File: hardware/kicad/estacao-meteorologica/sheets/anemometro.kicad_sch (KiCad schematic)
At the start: 12 parts, among them J31 R-RJ11R06P-A800, U40 SN74LVC1G17DBVR

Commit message: refatoracao: atualizacoes de hardware e falta revisao LoRa
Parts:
- added R42: 1k, Resistor_SMD:R_0603_1608Metric, symbol Device:R
- C40: value 10n -> 100n; Function Filtro do reed -> Filtro RC do reed com R41; suprime bounce e ruido de alta f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
- D41: Function Clamp secundario para GND e 3V3 -> Clamp secundario: p1=GND, p2=+3V3, p3=sinal filtrado
- J31: Function RJ11 individual; contatos centrais -> Conector do anemometro; reed externo entre p3 e p4; Rating 6P6C; p3=return; p4=signal; THT -> 6P6C; p3=+3V3 via R42; p4=sinal; THT
- R40: Function Pull-up ANTES do resistor serie; reed fechado ~0V -> Pull-down do sinal bruto; reed aberto = nivel baixo
- R41: Function Limitacao de corrente e filtro RC -> Resistor serie: limita corrente de clamp e, com C40, filtra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
- TP40: Function ANEMOMETRO_RAW -> Ponto de teste do sinal bruto ANEMOMETRO_RAW; LCSC (none) -> N/A (pad PCB); LCSC Part (none) -> N/A (pad PCB); MPN (none) -> TestPoint_Pad_D1.5mm; Manufacturer (none) -> PCB
- TP41: Function ANEMOMETRO_FILT -> Ponto de teste do sinal filtrado ANEMOMETRO_FILT; LCSC (none) -> N/A (pad PCB); LCSC Part (none) -> N/A (pad PCB); MPN (none) -> TestPoint_Pad_D1.5mm; Manufacturer (none) -> PCB
- TP42: Function WIND_SPEED_PULSE -> Ponto de teste da saida digital WIND_SPEED_PULSE; LCSC (none) -> N/A (pad PCB); LCSC Part (none) -> N/A (pad PCB); MPN (none) -> TestPoint_Pad_D1.5mm; Manufacturer (none) -> PCB
- TP43: Function GND -> Ponto de teste de referencia GND; LCSC (none) -> N/A (pad PCB); LCSC Part (none) -> N/A (pad PCB); MPN (none) -> TestPoint_Pad_D1.5mm; Manufacturer (none) -> PCB
- U40: Function Schmitt nao inversor; reed fecha -> borda de descida -> Schmitt nao inversor; reed fecha -> borda de subida em WIND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
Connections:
- net +3V3: now also R42.2; no longer R40.1
- net GND: now also R40.1; no longer J31.3
- new net: J31.3, R42.1
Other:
- note added: "1 CONECTOR / ESD / REFERENCIA"
- note added: "2 FILTRO / CLAMP SECUNDARIO"
- note added: "D40 deve ficar junto ao RJ11; R41, D41 e C40 junto ao U40. Manter plano GND continuo e retorno curto para D40. D40 e a protecao primaria do cabo; D41 apenas limita o residuo no buffer. Sem isolamento ou qualificacao contra raios: validar transitorios em bancada."
- note added: "Interface do sensor: J31.3 fornece +3V3 atraves de R42=1k; o reed externo fecha entre p3 e p4. R40=10k e o pull-down: reed aberto = 0 V; reed fechado = ~3,0 V e saida alta. C40=100n: tau de subida ~0,56 ms e de descida ~1,47 ms. PENDENCIA DE FIRMWARE: usar EXTI na subida e sem pull interno; o codigo atual ainda usa descida com pull-up. Debounce <= 6 ms para 75 Hz."
- note added: "MISOL: contato reed passivo; cabo externo ~2 m. J31 p3 = +3V3 via R42; J31 p4 = sinal."
- note removed: "1 CONECTOR / ESD"
- note removed: "2 FILTRO / CLAMP"
- note removed: "ESD junto ao RJ11; clamp e C junto ao buffer. Plano GND continuo. Protecao transitoria a validar em bancada; sem isolamento e sem qualificacao contra raios."
- note removed: "MISOL: contato reed passivo; cabo externo ~2 m; entrada individual 6P6C p3/p4."
- note removed: "Pull-up no lado do cabo evita divisor 4k7/10k na entrada Schmitt. Tau abertura=147 us; fechamento=47 us. Debounce atual: 20 ms limita f ~50 Hz. Com 2,4 km/h/Hz: 50 m/s exige 75 Hz; revisar debounce no firmware."
- moved on the sheet: R40, TP42, TP43

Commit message: refatoracao: lora + Verificacao projeto inteiro
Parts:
- C40: LCSC C57112 -> C14663; LCSC Part C57112 -> C14663; MPN 0603B103K500NT -> CC0603KRX7R9BB104; Manufacturer FH -> YAGEO; Modelo 3D (none) -> ${KICAD9_3DMODEL_DIR}/Capacitor_SMD.3dshapes/C_0603_1608Met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; Status_Ficha (none) -> Conferido no catalogo em 2026-09-24; verificar estoque ao c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
- C41: Modelo 3D (none) -> ${KICAD9_3DMODEL_DIR}/Capacitor_SMD.3dshapes/C_0603_1608Met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; Status_Ficha (none) -> Conferido no catalogo em 2026-09-24; verificar estoque ao c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
- D40: Modelo 3D (none) -> ${KICAD9_3DMODEL_DIR}/Diode_SMD.3dshapes/D_SOD-882.step; Status_Ficha (none) -> Conferido no catalogo em 2026-09-24; verificar estoque ao c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
- D41: Modelo 3D (none) -> ${KICAD9_3DMODEL_DIR}/Package_TO_SOT_SMD.3dshapes/SOT-23.st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; Status_Ficha (none) -> Conferido no catalogo em 2026-09-24; verificar estoque ao c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
- J31: Manufacturer Ckmtw -> Ckmtw(Shenzhen Cankemeng); Modelo 3D (none) -> ${KIPRJMOD}/../../libraries/Sensores_Meteo/Sensores_Meteo.3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; Status_Ficha (none) -> Conferido no catalogo em 2026-09-24; verificar estoque ao c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
- R40, R41: Manufacturer UNI-ROYAL -> UNI-ROYAL(Uniroyal Elec); Modelo 3D (none) -> ${KICAD9_3DMODEL_DIR}/Resistor_SMD.3dshapes/R_0603_1608Metr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; Status_Ficha (none) -> Conferido no catalogo em 2026-09-24; verificar estoque ao c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
- R42: LCSC C25804 -> C21190; LCSC Part C25804 -> C21190; MPN 0603WAF1002T5E -> 0603WAF1001T5E; Manufacturer UNI-ROYAL -> UNI-ROYAL(Uniroyal Elec); Modelo 3D (none) -> ${KICAD9_3DMODEL_DIR}/Resistor_SMD.3dshapes/R_0603_1608Metr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; Status_Ficha (none) -> Conferido no catalogo em 2026-09-24; verificar estoque ao c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
- TP40, TP41, TP42, TP43: LCSC N/A (pad PCB) -> N/A; LCSC Part N/A (pad PCB) -> N/A; MPN TestPoint_Pad_D1.5mm -> N/A - elemento de cobre da PCB; Manufacturer PCB -> N/A; Modelo 3D (none) -> N/A - geometria de cobre, sem corpo
- U40: Modelo 3D (none) -> ${KICAD9_3DMODEL_DIR}/Package_TO_SOT_SMD.3dshapes/SOT-23-5.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; Status_Ficha (none) -> Conferido no catalogo em 2026-09-24; verificar estoque ao c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

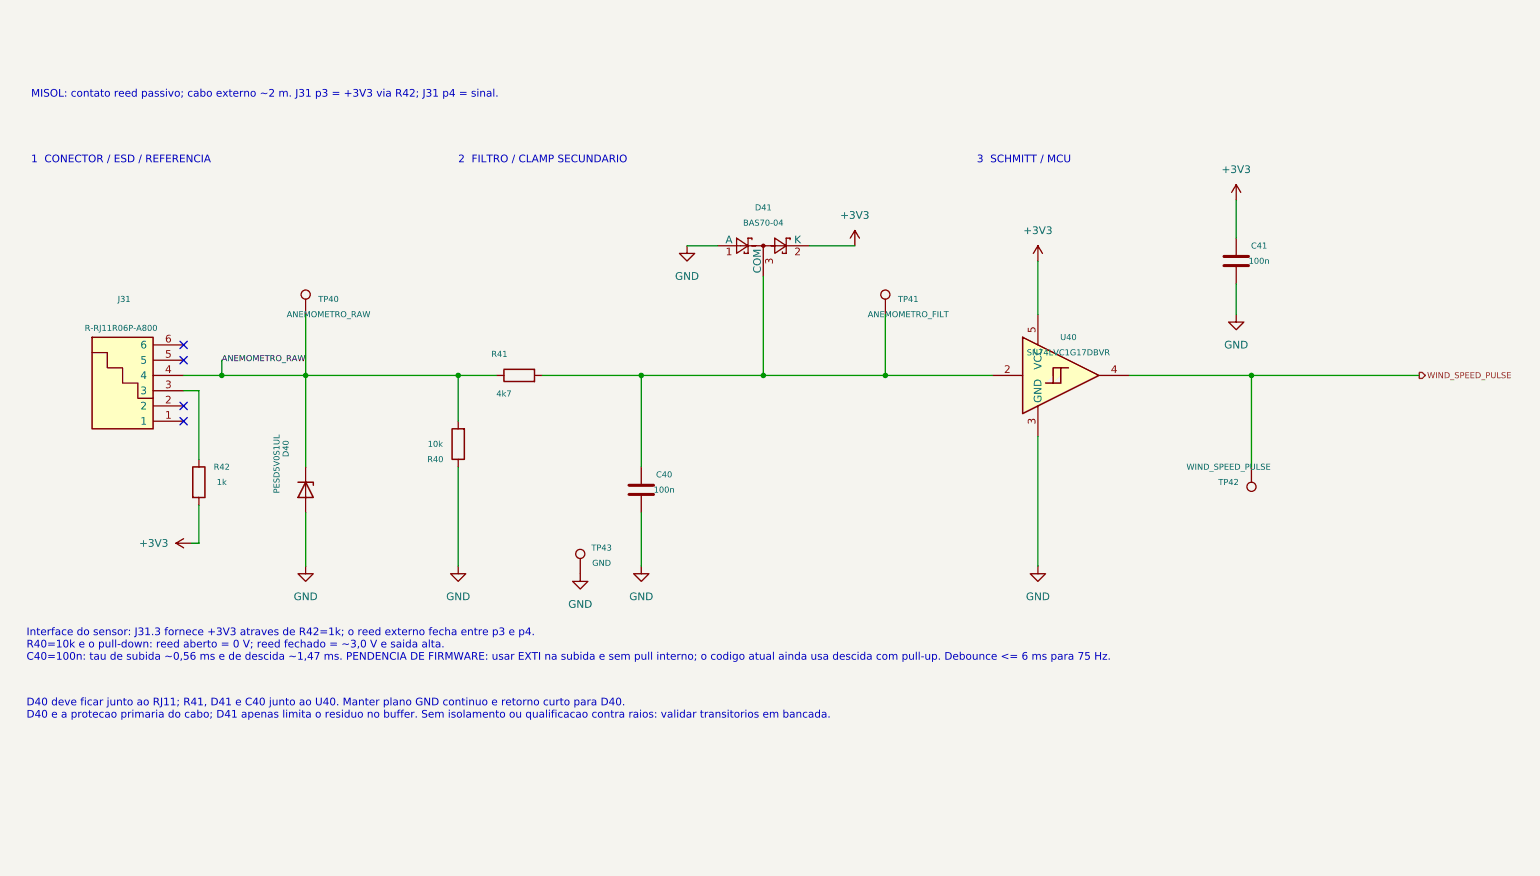
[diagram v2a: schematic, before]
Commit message: Padronizacao de nomes e numero de componentes
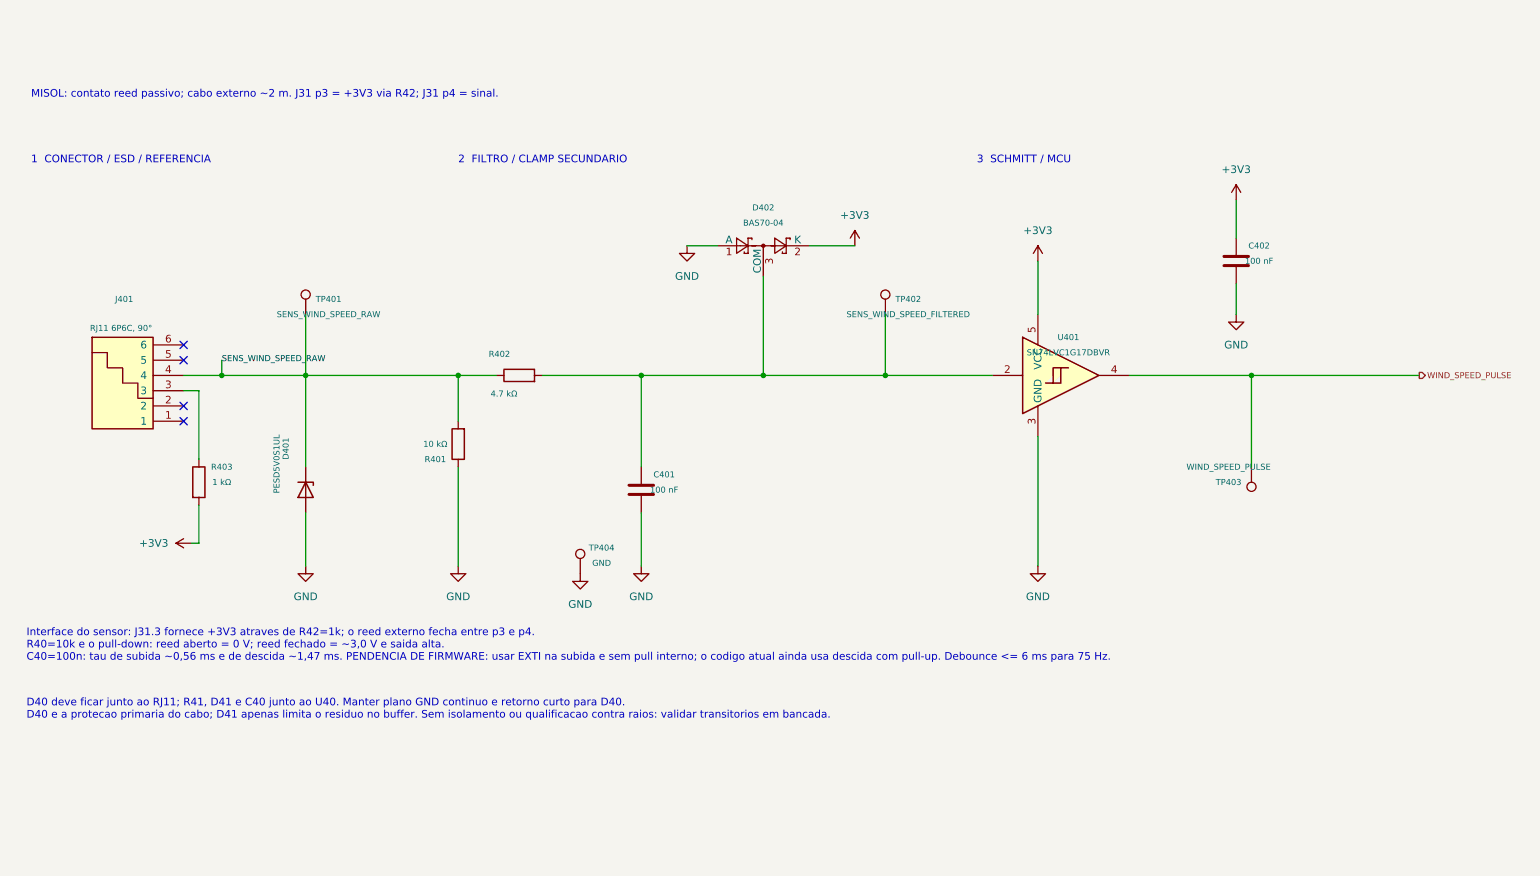
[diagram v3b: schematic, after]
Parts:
- C401: renamed from C40; value 100n -> 100 nF; Assembly (none) -> SMT; LCSC Part C14663 -> (none); Modelo 3D ${KICAD9_3DMODEL_DIR}/Capacitor_SMD.3dshapes/C_0603_1608Met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 -> (none); Rating 10%; 50V; X7R -> (none); Specification (none) -> 10%; 50V; X7R; Status_Ficha Conferido no catalogo em 2026-09-24; verificar estoque ao c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 -> (none); Verification (none) -> Conferido no catalogo em 2026-09-24; verificar estoque ao c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
- C402: renamed from C41; value 100n -> 100 nF; Assembly (none) -> SMT; LCSC Part C14663 -> (none); Modelo 3D ${KICAD9_3DMODEL_DIR}/Capacitor_SMD.3dshapes/C_0603_1608Met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 -> (none); Rating 10%; 50V; X7R -> (none); Specification (none) -> 10%; 50V; X7R; Status_Ficha Conferido no catalogo em 2026-09-24; verificar estoque ao c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 -> (none); Verification (none) -> Conferido no catalogo em 2026-09-24; verificar estoque ao c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
- D401: renamed from D40; Assembly (none) -> SMT; LCSC Part C85402 -> (none); Modelo 3D ${KICAD9_3DMODEL_DIR}/Diode_SMD.3dshapes/D_SOD-882.step -> (none); Rating VRWM=5V; IR max 1uA at 5V/25C; see datasheet -> (none); Specification (none) -> VRWM=5V; IR max 1uA at 5V/25C; see datasheet; Status_Ficha Conferido no catalogo em 2026-09-24; verificar estoque ao c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 -> (none); Verification (none) -> Conferido no catalogo em 2026-09-24; verificar estoque ao c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
- D402: renamed from D41; Assembly (none) -> SMT; LCSC Part C389351 -> (none); Modelo 3D ${KICAD9_3DMODEL_DIR}/Package_TO_SOT_SMD.3dshapes/SOT-23.st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 -> (none); Rating IR max 100nA at 50V/25C; 1=GND, 2=3V3, 3=signal -> (none); Specification (none) -> IR max 100nA at 50V/25C; 1=GND, 2=3V3, 3=signal; Status_Ficha Conferido no catalogo em 2026-09-24; verificar estoque ao c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 -> (none); Verification (none) -> Conferido no catalogo em 2026-09-24; verificar estoque ao c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
- J401: renamed from J31; value R-RJ11R06P-A800 -> RJ11 6P6C, 90°; Assembly (none) -> SMT; LCSC Part C189750 -> (none); Modelo 3D ${KIPRJMOD}/../../libraries/Sensores_Meteo/Sensores_Meteo.3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 -> (none); Rating 6P6C; p3=+3V3 via R42; p4=sinal; THT -> (none); Specification (none) -> 6P6C; p3=+3V3 via R42; p4=sinal; THT; Status_Ficha Conferido no catalogo em 2026-09-24; verificar estoque ao c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 -> (none); Verification (none) -> Conferido no catalogo em 2026-09-24; verificar estoque ao c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
- R401: renamed from R40; value 10k -> 10 kΩ; Assembly (none) -> SMT; LCSC Part C25804 -> (none); Modelo 3D ${KICAD9_3DMODEL_DIR}/Resistor_SMD.3dshapes/R_0603_1608Metr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 -> (none); Rating 1%; 0.1W; 75V -> (none); Specification (none) -> 1%; 0.1W; 75V; Status_Ficha Conferido no catalogo em 2026-09-24; verificar estoque ao c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 -> (none); Verification (none) -> Conferido no catalogo em 2026-09-24; verificar estoque ao c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
- R402: renamed from R41; value 4k7 -> 4.7 kΩ; Assembly (none) -> SMT; LCSC Part C23162 -> (none); Modelo 3D ${KICAD9_3DMODEL_DIR}/Resistor_SMD.3dshapes/R_0603_1608Metr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 -> (none); Rating 1%; 0.1W; 75V -> (none); Specification (none) -> 1%; 0.1W; 75V; Status_Ficha Conferido no catalogo em 2026-09-24; verificar estoque ao c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 -> (none); Verification (none) -> Conferido no catalogo em 2026-09-24; verificar estoque ao c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
- R403: renamed from R42; value 1k -> 1 kΩ; Assembly (none) -> SMT; LCSC Part C21190 -> (none); Modelo 3D ${KICAD9_3DMODEL_DIR}/Resistor_SMD.3dshapes/R_0603_1608Metr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 -> (none); Rating 1%; 0.1W; 75V -> (none); Specification (none) -> 1%; 0.1W; 75V; Status_Ficha Conferido no catalogo em 2026-09-24; verificar estoque ao c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 -> (none); Verification (none) -> Conferido no catalogo em 2026-09-24; verificar estoque ao c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
- TP401: renamed from TP40; value ANEMOMETRO_RAW -> SENS_WIND_SPEED_RAW; Assembly (none) -> PCB — sem compra; LCSC Part N/A -> (none); Modelo 3D N/A - geometria de cobre, sem corpo -> (none); Rating Copper pad; no purchased component -> (none); Specification (none) -> Copper pad; no purchased component
- TP402: renamed from TP41; value ANEMOMETRO_FILT -> SENS_WIND_SPEED_FILTERED; Assembly (none) -> PCB — sem compra; LCSC Part N/A -> (none); Modelo 3D N/A - geometria de cobre, sem corpo -> (none); Rating Copper pad; no purchased component -> (none); Specification (none) -> Copper pad; no purchased component
- TP403: renamed from TP42; Assembly (none) -> PCB — sem compra; LCSC Part N/A -> (none); Modelo 3D N/A - geometria de cobre, sem corpo -> (none); Rating Copper pad; no purchased component -> (none); Specification (none) -> Copper pad; no purchased component
- TP404: renamed from TP43; Assembly (none) -> PCB — sem compra; LCSC Part N/A -> (none); Modelo 3D N/A - geometria de cobre, sem corpo -> (none); Rating Copper pad; no purchased component -> (none); Specification (none) -> Copper pad; no purchased component
- U401: renamed from U40; Assembly (none) -> SMT; LCSC Part C7836 -> (none); Modelo 3D ${KICAD9_3DMODEL_DIR}/Package_TO_SOT_SMD.3dshapes/SOT-23-5.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 -> (none); Rating Non-inverting Schmitt; 1=NC 2=A 3=GND 4=Y 5=VCC -> (none); Specification (none) -> Non-inverting Schmitt; 1=NC 2=A 3=GND 4=Y 5=VCC; Status_Ficha Conferido no catalogo em 2026-09-24; verificar estoque ao c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 -> (none); Verification (none) -> Conferido no catalogo em 2026-09-24; verificar estoque ao c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
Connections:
- net ANEMOMETRO_RAW renamed SENS_WIND_SPEED_RAW

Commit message: Roteamento 2.0 - rj11 compartilhado biruta e anemometro
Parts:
- removed J401: RJ11 6P6C, 90°, Sensores_Meteo:RJ11-TH_PCB-6P6C-90, symbol Sensores_Meteo:PCB-6P6C-90
- removed R403: 1 kΩ, Resistor_SMD:R_0603_1608Metric, symbol Device:R
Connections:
- no-connect marks 4 -> 0

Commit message: Refact - mudança do sensor bh1750 para placa filha e conector jst + reposicionamento do sensor DHT22 para reduzir influencia de temperatura interna da placa
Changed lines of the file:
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@@
-	)
-	(junction
-		(at 52.07 80.01)
-		(diameter 0)
-		(color 0 0 0 0)
 	)
 	(junction
@@
 	(wire
 		(pts
-			(xy 52.07 80.01) (xy 66.04 80.01)
-		)
-		(stroke
-			(width 0)
-			(type default)
-		)
-	)
-	(wire
-		(pts
 			(xy 121.92 102.87) (xy 121.92 111.76)
 		)
@@
 	(wire
 		(pts
-			(xy 52.07 77.47) (xy 52.07 80.01)
-		)
-		(stroke
-			(width 0)
-			(type default)
-		)
-	)
-	(wire
-		(pts
 			(xy 121.92 80.01) (xy 121.92 95.25)
 		)
@@
 	(wire
 		(pts
-			(xy 45.72 80.01) (xy 52.07 80.01)
+			(xy 45.72 80.01) (xy 66.04 80.01)
 		)
 		(stroke
@@
 		)
 	)
-	(label "SENS_WIND_SPEED_RAW"
-		(at 52.07 77.47 0)
-		(effects
-			(font
-				(size 1 1)
-			)
-			(justify left)
-		)
-	)

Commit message: Add test points necessarios para debug
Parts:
- TP401, TP402, TP403: footprint TestPoint:TestPoint_Pad_D1.5mm -> TestPoint:TestPoint_Pad_D1.0mm
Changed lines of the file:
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@@
 			)
 		)
-		(property "Footprint" "TestPoint:TestPoint_Pad_D1.5mm"
+		(property "Footprint" "TestPoint:TestPoint_Pad_D1.0mm"
 			(at 66.04 69.85 0)
 			(effects
@@
 			)
 		)
-		(property "Description" "Ponto de teste em cobre, pad circular de 1,5 mm; rede ANEMOMETRO_RAW"
+		(property "Description" "Ponto de teste em cobre, pad circular de 1,0 mm; rede ANEMOMETRO_RAW"
 			(at 66.04 69.85 0)
 			(effects
@@
 			)
 		)
-		(property "Footprint" "TestPoint:TestPoint_Pad_D1.5mm"
+		(property "Footprint" "TestPoint:TestPoint_Pad_D1.0mm"
 			(at 162.56 69.85 0)
 			(effects
@@
 			)
 		)
-		(property "Description" "Ponto de teste em cobre, pad circular de 1,5 mm; rede ANEMOMETRO_FILT"
+		(property "Description" "Ponto de teste em cobre, pad circular de 1,0 mm; rede ANEMOMETRO_FILT"
 			(at 162.56 69.85 0)
 			(effects
@@
 			)
 		)
-		(property "Footprint" "TestPoint:TestPoint_Pad_D1.5mm"
+		(property "Footprint" "TestPoint:TestPoint_Pad_D1.0mm"
 			(at 223.52 95.25 0)
 			(effects
@@
 			)
 		)
-		(property "Description" "Ponto de teste em cobre, pad circular de 1,5 mm; rede WIND_SPEED_PULSE"
+		(property "Description" "Ponto de teste em cobre, pad circular de 1,0 mm; rede WIND_SPEED_PULSE"
 			(at 223.52 95.25 0)
 			(effects

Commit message: feat(hardware): consolida revisão PCB V2
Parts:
- TP404: footprint TestPoint:TestPoint_Pad_D1.5mm -> TestPoint:TestPoint_Pad_D1.0mm
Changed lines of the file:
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@@
 			)
 		)
-		(property "Footprint" "TestPoint:TestPoint_Pad_D1.5mm"
+		(property "Footprint" "TestPoint:TestPoint_Pad_D1.0mm"
 			(at 111.76 113.03 0)
 			(effects
